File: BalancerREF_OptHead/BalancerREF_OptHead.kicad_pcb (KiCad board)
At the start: 2 copper layers, 25 x 50 mm, 27 parts, among them J5 TO MAIN BOARD, Q1 AO3400A, U4 TS3021IYLT, U8 TLV9062IDR

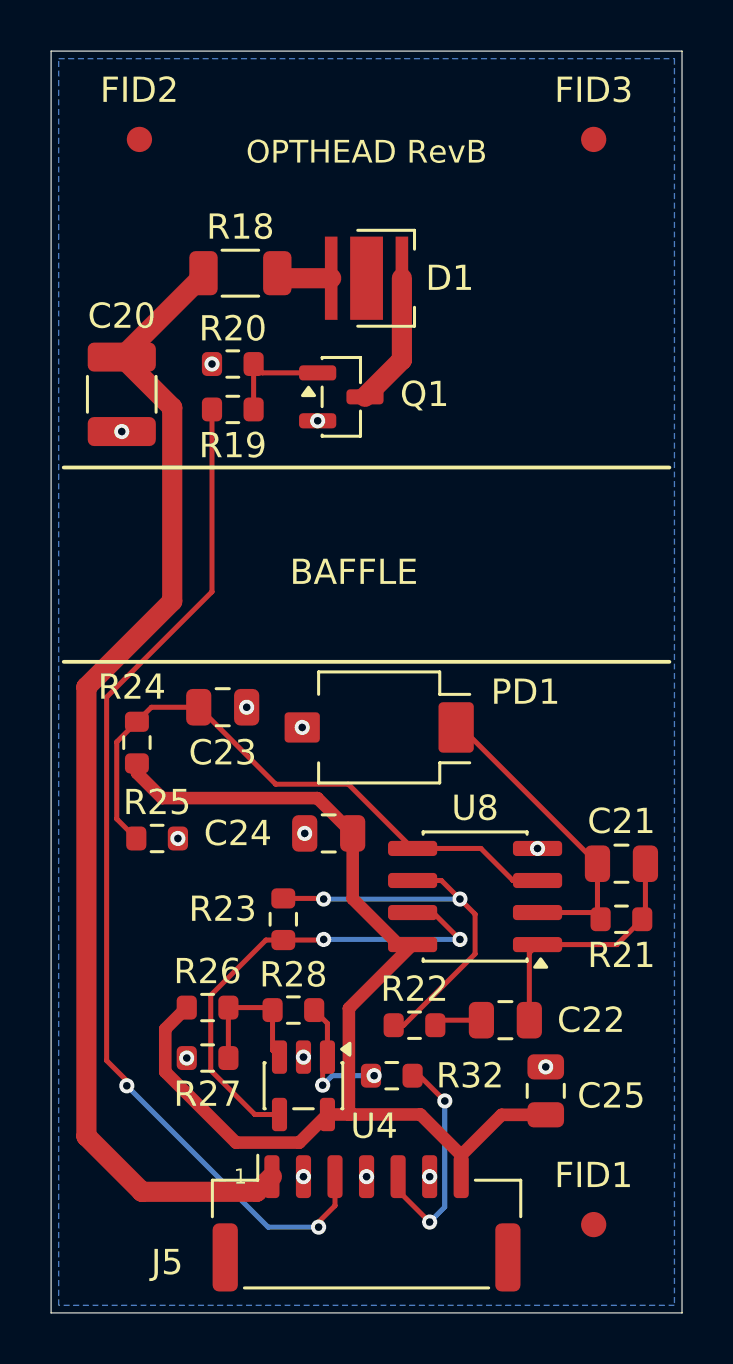
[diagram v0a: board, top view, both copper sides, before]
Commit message: feat: BalancerCarrier on a FeatherS3[D], and two board fixes
Adds BalancerCarrier: the HOBOVibe instrument rebuilt as a carrier around an
Unexpected Maker FeatherS3[D] (ESP32-S3, 16 MB flash, 8 MB QSPI PSRAM), so the
MCU, LiPo charger, fuel gauge and USB come from a proven module instead of being
respun. 31 parts, ERC 0 violations.

The module is a Feather, so U1 uses Module:Adafruit_Feather-compatible geometry -
Unexpected Maker's own 28-pad footprint and symbol, checked pin-for-pin against
their FeatherS3[D] schematic headers J1 and JP3. That makes the footprint
vendor-independent: another Feather drops in without a respin, which is the
exposure that bit this project when the DFR0975 went pre-order only.

Seven parts came out once the module's own hardware was traced properly. LDO2
(NCP167BMX330TBG, 700 mA) is fed from VBUS, which ORs USB and VBAT, so it is live
on battery and powers the GPS - the discrete load switch went. The onboard
MAX17048 fuel gauge reads the cell directly over I2C, so the supply-sense divider
went with it.

Board fixes, both found by diffing against BalancerREF rather than trusting what
was drawn:

  BalancerREF  R30/C28 100k/1n -> 10k/10n. TI SCES586E section 5.8 characterises
               10k/10n at tw 100-110 us across all four supply voltages; 100k is
               ten times beyond the largest Rext TI characterises.

  OptHead      PD1 BPW34S -> SFH 2440. The old line was unbuildable: an SMD
               footprint against Vishay's BPW34S, which doc 81521 calls "leaded",
               naming an Osram part that is out of production. SFH 2440 is
               pad-identical, peaks at 620 nm against the 625 nm emitter, and
               blocks the IR the BPW34 was most sensitive to. C21 10 pF -> 22 pF:
               junction capacitance roughly doubles, so Cf_min rises to ~12.3 pF
               and the fitted 10 pF would peak. NOT SFH 2430 - 200 us rise time.

PhotoTach-BOM.csv rebuilt. It had nine classes of error, the worst struc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
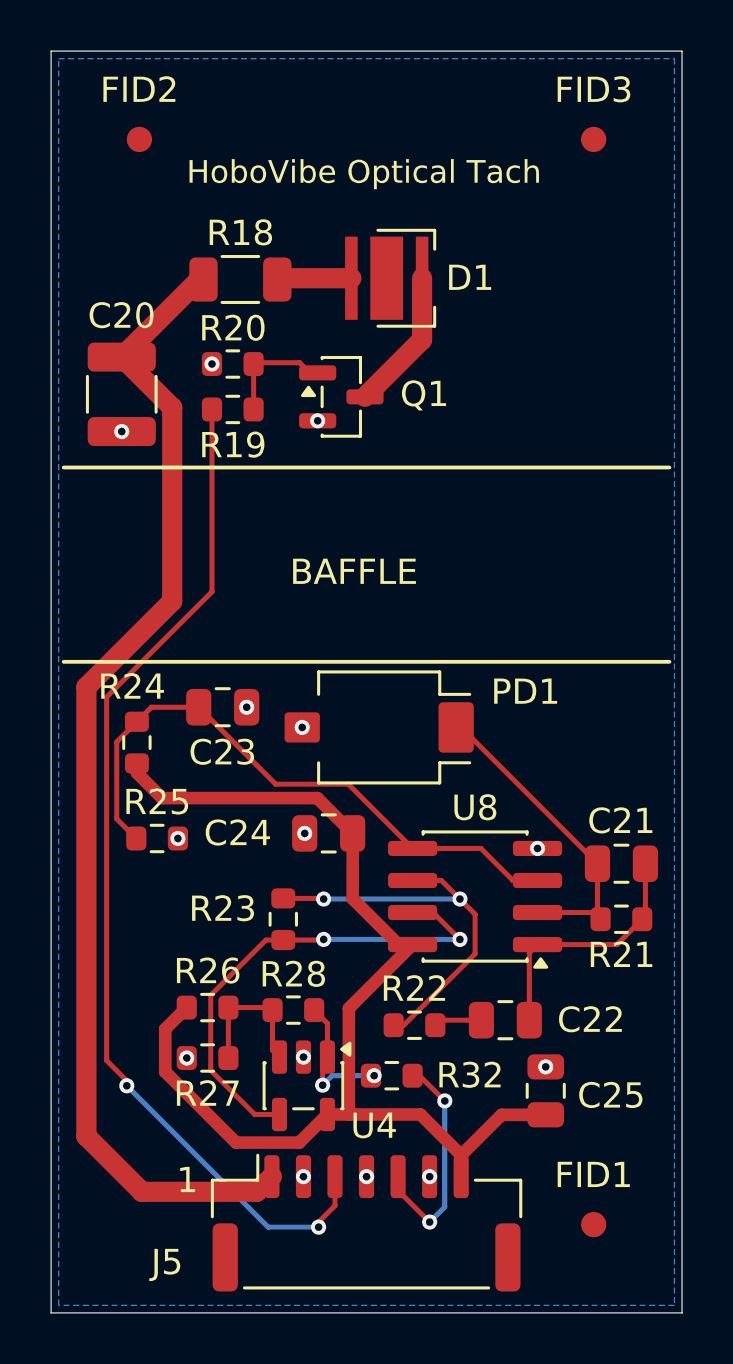
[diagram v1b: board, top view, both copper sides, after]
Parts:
- C21: value 10p C0G -> 22p C0G
- PD1: value BPW34S -> SFH 2440; footprint Osram_BPW34S-SMD -> Osram_SFH2440
- moved D1 0.80 mm to (113.3, 109.0)
- moved R18 0.25 mm to (107.5, 109.0)
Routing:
- net Net-(D1-A): track 2.22 -> 2.96 mm
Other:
- board text added: "HoboVibe Optical Tach"
- board text removed: "OPTHEAD RevB"
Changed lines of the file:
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@@
 	(footprint "R_1206_3216Metric"
 		(layer "F.Cu")
-		(at 107.5 108.8)
+		(at 107.5 109.05)
 		(descr "Resistor SMD 1206 (3216 Metric), square (rectangular) end terminal, IPC-7351 nominal, (Body size source: IPC-SM-782 page 72, https://www.pcb-3d.com/wordpress/wp-content/uploads/ipc-sm-782a_amendment_1_and_2.pdf)")
 		(tags "resistor")
@@
 	(footprint "LED_Cree-XP"
 		(layer "F.Cu")
-		(at 112.5 109 180)
+		(at 113.3 109 180)
 		(descr "LED Cree-XP http://www.cree.com/~/media/Files/Cree/LED-Components-and-Modules/XLamp/Data-and-Binning/XLampXPE2.pdf")
 		(tags "LED Cree XP")
@@
 		)
 	)
-	(footprint "Osram_BPW34S-SMD"
+	(footprint "Osram_SFH2440"
 		(layer "F.Cu")
 		(at 113 126.8 180)
@@
 			)
 		)
-		(property "Value" "BPW34S"
+		(property "Value" "SFH 2440"
 			(at 0 3.17 180)
 			(layer "F.Fab")
@@
 			)
 		)
-		(property "Value" "10p C0G"
+		(property "Value" "22p C0G"
 			(at 0 1.68 0)
 			(layer "F.Fab")
@@
 		(layer "Edge.Cuts")
 	)
+	(gr_text "HoboVibe Optical Tach"
+		(at 112.4 104.8 0)
+		(layer "F.SilkS")
+		(effects
+			(font
+				(size 0.9 0.9)
+				(thickness 0.13)
+			)
+		)
+	)
+	(gr_text "1"
+		(at 105.4 144.75 0)
+		(layer "F.SilkS")
+		(effects
+			(font
+				(size 1 1)
+				(thickness 0.1)
+			)
+		)
+	)
 	(gr_text "BAFFLE"
 		(at 112 120.65 0)
@@
 	)
 	(segment
-		(start 108.375 112.75)
-		(end 108.025 112.4)
+		(start 110.25 112.75)
+		(end 109.85 112.35)
 		(width 0.2)
 		(layer "F.Cu")
@@
 	(segment
 		(start 110.5625 112.75)
-		(end 108.375 112.75)
+		(end 110.25 112.75)
+		(width 0.2)
+		(layer "F.Cu")
+		(net "/MOS_GATE")
+	)
+	(segment
+		(start 109.85 112.35)
+		(end 108.075 112.35)
+		(width 0.2)
+		(layer "F.Cu")
+		(net "/MOS_GATE")
+	)
+	(segment
+		(start 108.075 112.35)
+		(end 108.025 112.4)
 		(width 0.2)
 		(layer "F.Cu")
@@
 	)
 	(segment
-		(start 113.9 109)
-		(end 113.9 112.2375)
+		(start 112.4375 113.7)
+		(end 114.7 111.4375)
 		(width 0.8)
 		(layer "F.Cu")
@@
 	)
 	(segment
-		(start 113.9 112.2375)
-		(end 112.4375 113.7)
+		(start 114.7 111.4375)
+		(end 114.7 109)
 		(width 0.8)
 		(layer "F.Cu")
@@
 	)
 	(segment
+		(start 105.875 109.05)
+		(end 102.8 112.125)
+		(width 0.8)
+		(layer "F.Cu")
+		(net "/SYS_SW")
+	)
+	(segment
 		(start 101.4 143)
 		(end 103.6 145.2)
@@
 	)
 	(segment
-		(start 106.0375 108.8)
-		(end 106.0375 108.8875)
-		(width 0.8)
-		(layer "F.Cu")
-		(net "/SYS_SW")
-	)
-	(segment
-		(start 106.0375 108.8875)
-		(end 102.8 112.125)
-		(width 0.8)
-		(layer "F.Cu")
-		(net "/SYS_SW")
-	)
-	(segment
 		(start 104.8 114.125)
 		(end 104.8 121.8)
@@
 	)
 	(segment
-		(start 109.1625 109)
-		(end 108.9625 108.8)
+		(start 106.0375 109.05)
+		(end 105.875 109.05)
+		(width 0.8)
+		(layer "F.Cu")
+		(net "/SYS_SW")
+	)
+	(segment
+		(start 109.0125 109)
+		(end 108.9625 109.05)
 		(width 0.8)
 		(layer "F.Cu")
@@
 	)
 	(segment
-		(start 111.1 109)
-		(end 109.1625 109)
+		(start 111.9 109)
+		(end 109.0125 109)
 		(width 0.8)
 		(layer "F.Cu")
@@
 			)
 		)
-	)
-	(gr_text "OPTHEAD RevB"
-		(at 112.5 104.0 0)
-		(layer "F.SilkS")
-		(effects
-			(font
-				(size 0.9 0.9)
-				(thickness 0.13)
-			)
-		)
-	)
-	(gr_text "1"
-		(at 107.5 144.6 0)
-		(layer "F.SilkS")
-		(effects
-			(font
-				(size 0.6 0.6)
-				(thickness 0.1)
-			)
-		)

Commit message: feat: carrier PCB first layout, schematic fixes, OptHead 3D models
BalancerCarrier
  - First .kicad_pcb into git: 4 layers, 139 tracks, 51 vias, GND on In1.Cu
    and +3V3 on In2.Cu, 0 unconnected. Placement recovered from
    temp-freerouting.dsn after the Freerouting crash took the board file.
  - Schematic fixes found in review: LED1 was wired backwards (cathode on the
    GPIO), R13 sat in series with J5.5 instead of returning to GND, and
    GPS_UART_RX collided with the module I2C bus on IO9 - moved to IO7.
  - The GPS block is kept but DNP for the first round; the board is a
    proof-of-concept that the balancer works before the GPS is added on.
  - .kicad_pro carries the netclasses the board's DRC depends on, so it goes
    in with the board rather than after it.
  - scripts/restore_placement_pcbnew.py is the recovery tool that worked.
    restore_placement_from_dsn.py is kept beside it with a header explaining
    why editing the file directly shears the pads: KiCad stores each pad's
    angle including its parent footprint's.

BalancerREF_OptHead
  - PD1 is now an SFH 2440. The SFH 2430 it replaces has a 200 us rise time
    against the 2440's 0.09 us, which cannot resolve a rotor blade passing.
  - 3D models attached to D1 and PD1.

Known, not fixed here: 13 DRC violations on the carrier, 12 of them U5's LGA
pad-to-pad gap of 0.150 mm against the 0.2 mm netclass clearance (needs a
local override, not a layout change), and one benign J3 THT layer mismatch.
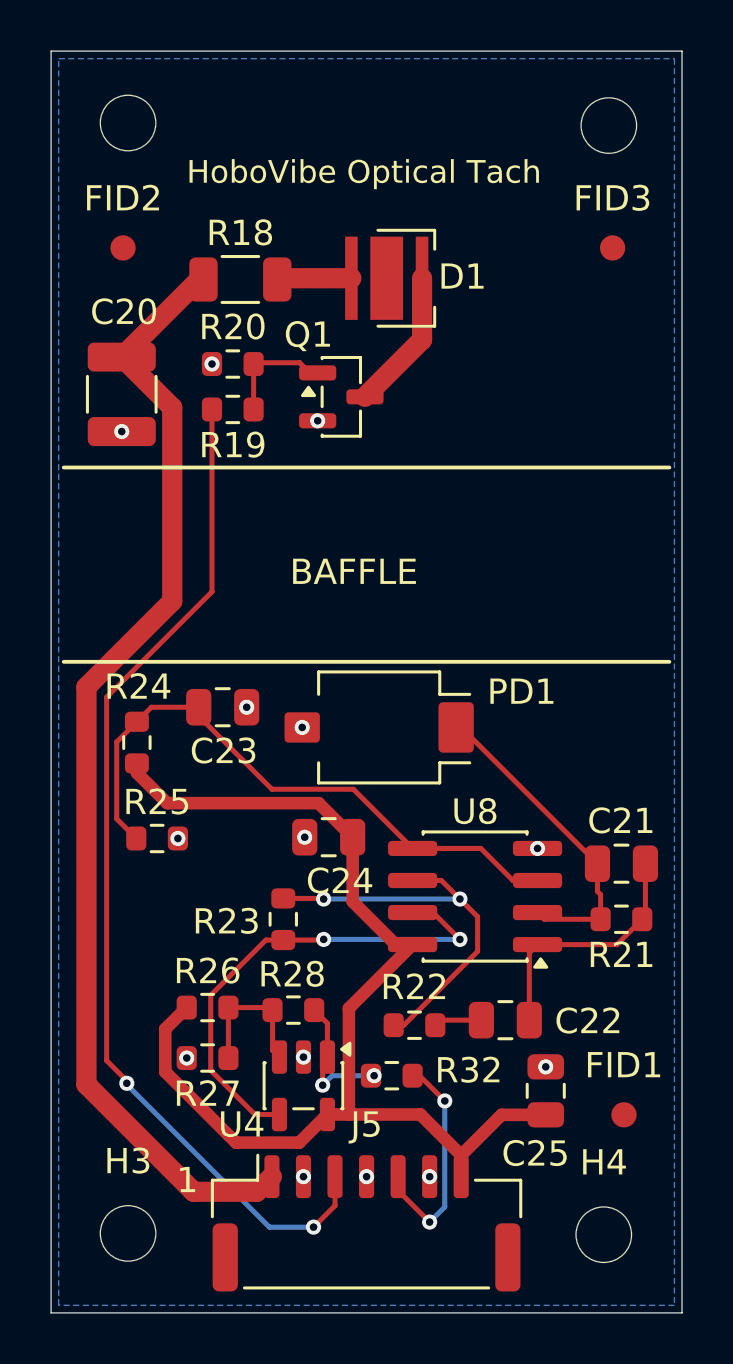
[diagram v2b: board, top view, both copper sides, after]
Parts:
- added H1: MountingHole, MountingHole:MountingHole_2.2mm_M2_DIN965, F.Cu at (103.0, 102.8)
- added H2: MountingHole, MountingHole:MountingHole_2.2mm_M2_DIN965, F.Cu at (122.1, 103.0)
- added H3: MountingHole, MountingHole:MountingHole_2.2mm_M2_DIN965, F.Cu at (103.0, 146.8)
- added H4: MountingHole, MountingHole:MountingHole_2.2mm_M2_DIN965, F.Cu at (121.9, 146.9)
- C20: footprint C_1210_3225Metric -> Capacitor_SMD:C_1210_3225Metric
- C21, C22, C23, C24, C25: footprint C_0805_2012Metric -> Capacitor_SMD:C_0805_2012Metric
- D1: footprint LED_Cree-XP -> LED_SMD:LED_Cree-XP
- J5: footprint JST_GH_SM07B-GHS-TB_1x07-1MP_P1.25mm_Horizontal -> Connector_JST:JST_GH_SM07B-GHS-TB_1x07-1MP_P1.25mm_Horizontal
- PD1: footprint Osram_SFH2440 -> OptoDevice:Osram_SFH2440
- Q1: footprint SOT-23 -> Package_TO_SOT_SMD:SOT-23
- R18: footprint R_1206_3216Metric -> Resistor_SMD:R_1206_3216Metric
- R19, R20, R21, R22, R23, R24, R25, R26, R27, R28, R32: footprint R_0603_1608Metric -> Resistor_SMD:R_0603_1608Metric
- U4: footprint SOT-23-5 -> Package_TO_SOT_SMD:SOT-23-5
- U8: footprint SOIC-8_3.9x4.9mm_P1.27mm -> Package_SO:SOIC-8_3.9x4.9mm_P1.27mm
- moved FID1 4.51 mm to (122.7, 142.2)
- moved FID3 4.36 mm to (122.2, 107.8)
- moved FID2 4.35 mm to (102.8, 107.8)
- moved C24 0.15 mm to (111.0, 131.2)
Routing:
- net /SYS_SW: track 46.1 -> 44.9 mm
